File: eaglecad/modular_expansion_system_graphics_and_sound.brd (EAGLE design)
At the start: 90.2 x 100 mm, 44 parts, among them IC1 74LS244N, IC8 74LS244N, IC9-74HCU04 74LS04N, J1-WAIT-AND-INT WAIT-AND-INT, J1_ADDRESS_CON j1, J2_DATA_AND_POWER_CON j2, J3-VIDEO-OUT RCA, J4-AUDIO-LEFT RCA, J5-AUDIO-RIGHT RCA, Q2 2N2222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

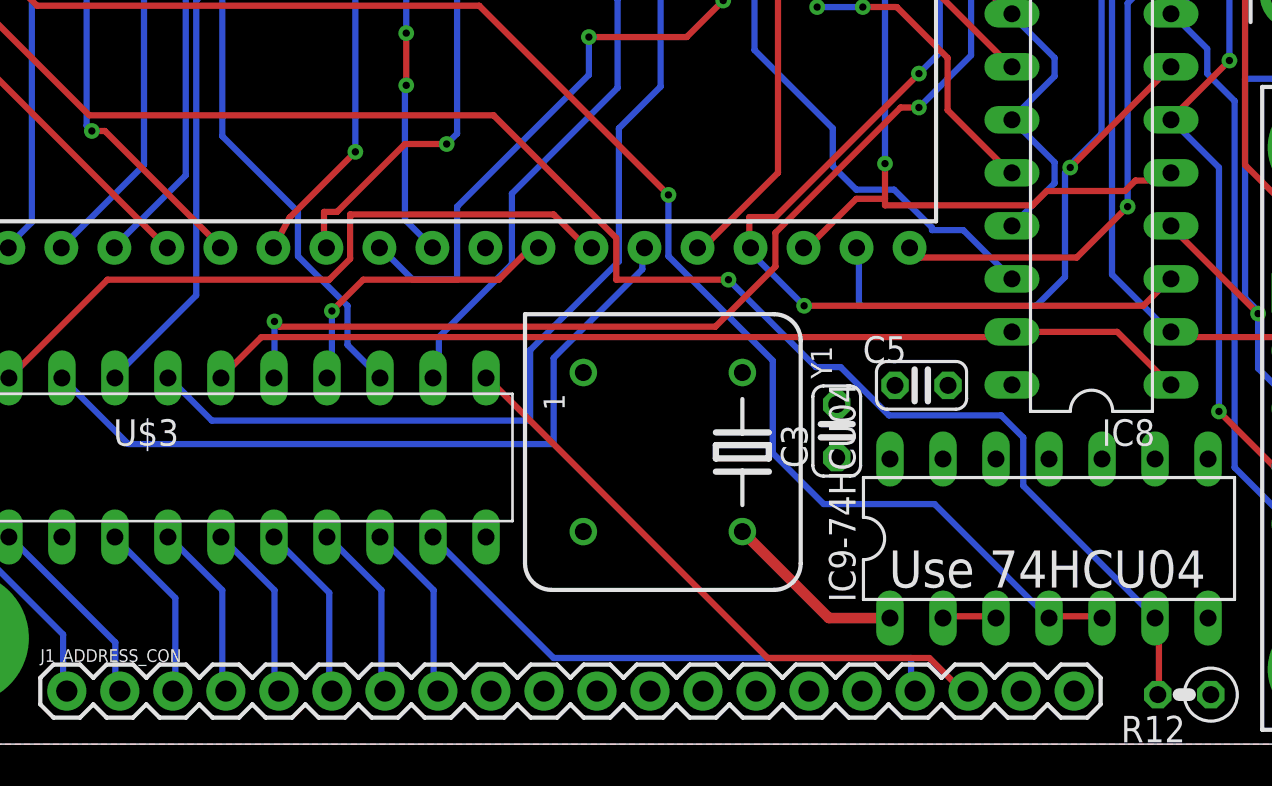
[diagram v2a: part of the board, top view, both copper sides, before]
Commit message: moved traces away from crystal module
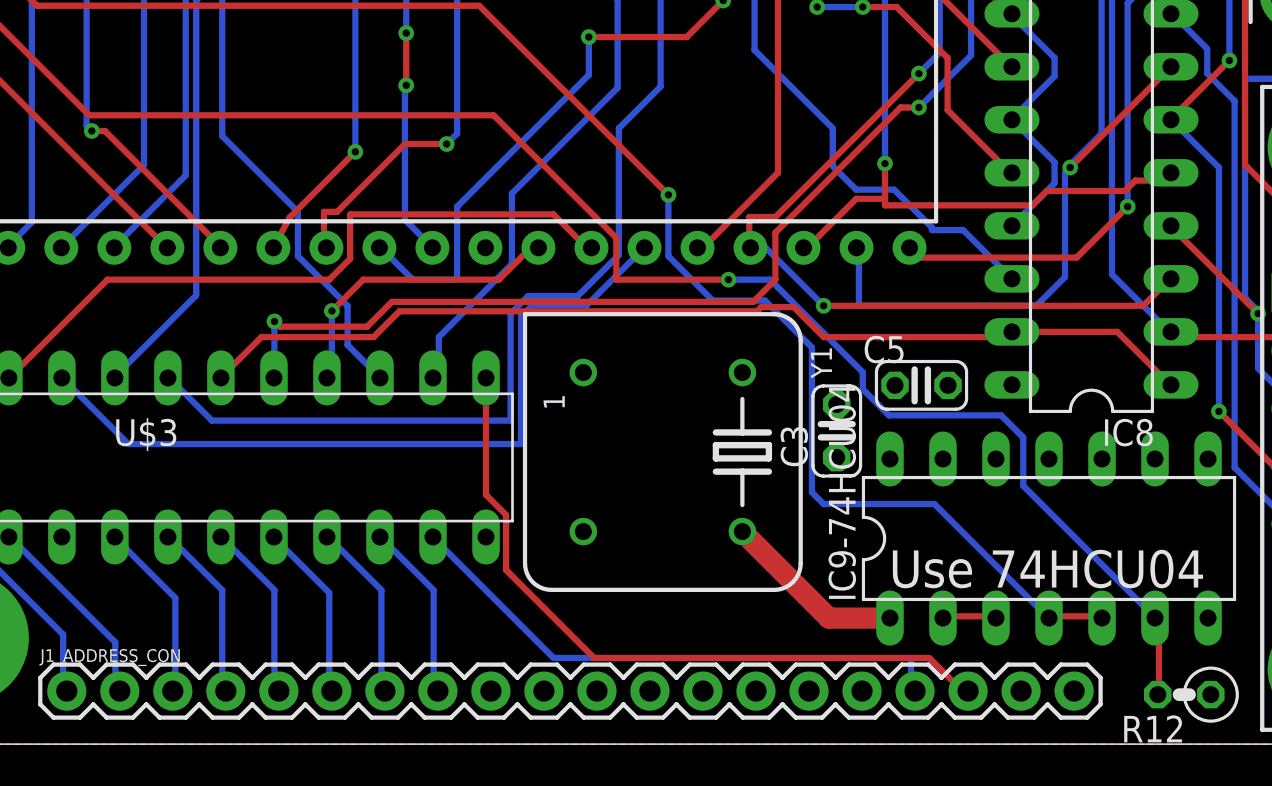
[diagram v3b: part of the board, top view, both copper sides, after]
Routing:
- net OUT*: track 29.3 -> 34.1 mm
- net CLK-IN-2: track 75.9 -> 77.3 mm
- net JOY1_IN_ENABLE_N: track 47.5 -> 48.7 mm
- net SND2_ENABLE_N: track 98.5 -> 99.3 mm
- net N$15: track 36.1 -> 36.7 mm
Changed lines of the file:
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@@
 <contactref element="J2_DATA_AND_POWER_CON" pad="20"/>
 <wire x1="70.625" y1="21" x2="71.875" y2="22.25" width="0.3" layer="1"/>
-<wire x1="54.375" y1="21" x2="70.625" y2="21" width="0.3" layer="1"/>
-<wire x1="51.875" y1="23.5" x2="54.375" y2="21" width="0.3" layer="16"/>
-<wire x1="51.875" y1="23.75" x2="51.875" y2="23.5" width="0.3" layer="16"/>
+<wire x1="55.3125" y1="21" x2="70.625" y2="21" width="0.3" layer="1"/>
+<wire x1="55.3125" y1="21" x2="52.535" y2="23.7775" width="0.3" layer="16"/>
+<wire x1="51.8075" y1="23.7775" x2="52.535" y2="23.7775" width="0.3" layer="16"/>
 <wire x1="71.875" y1="22.25" x2="71.9525" y2="22.29" width="0.3" layer="1"/>
-<wire x1="51.875" y1="23.75" x2="51.8075" y2="23.7775" width="0.3" layer="16"/>
 <wire x1="32.625" y1="68.625" x2="33.875" y2="67.375" width="0.3" layer="16"/>
 <wire x1="32.625" y1="78" x2="32.625" y2="68.625" width="0.3" layer="16"/>
@@
 <wire x1="51.75" y1="23.875" x2="51.8075" y2="23.7775" width="0.3" layer="1"/>
 <wire x1="64.125" y1="59.875" x2="64.14" y2="59.9175" width="0.3" layer="1"/>
-<via x="54.375" y="21" extent="1-16" drill="0.35"/>
+<via x="55.3125" y="21" extent="1-16" drill="0.35"/>
 <via x="65.75" y="85" extent="1-16" drill="0.35"/>
 <via x="59.875" y="32.125" extent="1-16" drill="0.35"/>
@@
 <contactref element="U$3" pad="18"/>
 <wire x1="28.375" y1="19.5" x2="26.5" y2="17.625" width="0.3" layer="1"/>
-<wire x1="64" y1="19.5" x2="28.375" y2="19.5" width="0.3" layer="1"/>
+<wire x1="64" y1="19.5" x2="56.25" y2="19.5" width="0.3" layer="1"/>
+<wire x1="56.25" y1="19.5" x2="55.3125" y2="19.5" width="0.3" layer="1"/>
+<wire x1="33.75" y1="19.5" x2="28.375" y2="19.5" width="0.3" layer="1"/>
 <wire x1="64.25" y1="19.75" x2="64" y2="19.5" width="0.3" layer="1"/>
 <wire x1="26.5" y1="17.625" x2="26.435" y2="17.5425" width="0.3" layer="1"/>
@@
 <wire x1="64.3325" y1="19.75" x2="69.375" y2="19.75" width="0.3" layer="1"/>
 <wire x1="71.875" y1="17.25" x2="71.9525" y2="17.21" width="0.3" layer="1"/>
+<wire x1="55.3125" y1="19.5" x2="53.875" y2="20.9375" width="0.3" layer="1"/>
+<wire x1="52.32729375" y1="20.9375" x2="52.12489375" y2="20.7351" width="0.3" layer="1"/>
+<wire x1="34.9851" y1="20.7351" x2="33.75" y2="19.5" width="0.3" layer="1"/>
+<wire x1="52.12489375" y1="20.7351" x2="34.9851" y2="20.7351" width="0.3" layer="1"/>
+<wire x1="53.875" y1="20.9375" x2="52.32729375" y2="20.9375" width="0.3" layer="1"/>
 </signal>
 <signal name="IN*">
@@
 <contactref element="J1_ADDRESS_CON" pad="18"/>
 <contactref element="U$3" pad="13"/>
-<wire x1="52.625" y1="4.125" x2="39.25" y2="17.5" width="0.3" layer="1"/>
-<wire x1="60.375" y1="4.125" x2="52.625" y2="4.125" width="0.3" layer="1"/>
+<wire x1="60.375" y1="4.125" x2="52.8125" y2="4.125" width="0.3" layer="1"/>
+<wire x1="52.8125" y1="4.125" x2="52.625" y2="4.125" width="0.3" layer="1"/>
 <wire x1="61.875" y1="2.625" x2="60.375" y2="4.125" width="0.3" layer="1"/>
 <wire x1="62.125" y1="2.625" x2="61.875" y2="2.625" width="0.3" layer="1"/>
-<wire x1="39.25" y1="17.5" x2="39.135" y2="17.5425" width="0.3" layer="1"/>
 <wire x1="62.125" y1="2.625" x2="62.23" y2="2.54" width="0.3" layer="1"/>
+<wire x1="52.625" y1="4.125" x2="44.3125" y2="4.125" width="0.3" layer="1"/>
+<wire x1="39.135" y1="11.94450625" x2="39.135" y2="17.5425" width="0.3" layer="1"/>
+<wire x1="40.0978" y1="8.3397" x2="40.0978" y2="10.98170625" width="0.3" layer="1"/>
+<wire x1="40.0978" y1="10.98170625" x2="39.135" y2="11.94450625" width="0.3" layer="1"/>
+<wire x1="44.3125" y1="4.125" x2="40.0978" y2="8.3397" width="0.3" layer="1"/>
 </signal>
 <signal name="VDP_MODE">
@@
 <contactref element="U$3" pad="21"/>
 <wire x1="22" y1="14.375" x2="18.875" y2="17.5" width="0.3" layer="16"/>
-<wire x1="42.375" y1="14.375" x2="22" y2="14.375" width="0.3" layer="16"/>
-<wire x1="42.375" y1="18.5" x2="42.375" y2="14.375" width="0.3" layer="16"/>
-<wire x1="46.625" y1="22.75" x2="42.375" y2="18.5" width="0.3" layer="16"/>
-<wire x1="46.625" y1="23.75" x2="46.625" y2="22.75" width="0.3" layer="16"/>
+<wire x1="22" y1="14.375" x2="40.8125" y2="14.375" width="0.3" layer="16"/>
+<wire x1="46.625" y1="23.6875" x2="46.625" y2="23.75" width="0.3" layer="16"/>
 <wire x1="18.875" y1="17.5" x2="18.815" y2="17.5425" width="0.3" layer="16"/>
 <wire x1="46.625" y1="23.75" x2="46.7275" y2="23.7775" width="0.3" layer="16"/>
+<wire x1="40.8125" y1="20.48520625" x2="41.34364375" y2="21.01635" width="0.3" layer="16"/>
+<wire x1="41.34364375" y1="21.01635" x2="43.95385" y2="21.01635" width="0.3" layer="16"/>
+<wire x1="40.8125" y1="14.375" x2="40.8125" y2="20.48520625" width="0.3" layer="16"/>
+<wire x1="43.95385" y1="21.01635" x2="46.625" y2="23.6875" width="0.3" layer="16"/>
 </signal>
 <signal name="UP1">
@@
 <wire x1="29" y1="20.25" x2="29" y2="17.625" width="0.3" layer="16"/>
 <wire x1="29.25" y1="20" x2="29" y2="20.25" width="0.3" layer="1"/>
-<wire x1="50.125" y1="20" x2="29.25" y2="20" width="0.3" layer="1"/>
-<wire x1="53" y1="22.875" x2="50.125" y2="20" width="0.3" layer="1"/>
-<wire x1="53" y1="24.5" x2="53" y2="22.875" width="0.3" layer="1"/>
+<wire x1="33.4375" y1="20" x2="29.25" y2="20" width="0.3" layer="1"/>
+<wire x1="53" y1="22.25" x2="51.9375" y2="21.1875" width="0.3" layer="1"/>
+<wire x1="53" y1="24.5" x2="53" y2="22.25" width="0.3" layer="1"/>
 <wire x1="59" y1="30.5" x2="53" y2="24.5" width="0.3" layer="1"/>
 <wire x1="59.875" y1="30.5" x2="59" y2="30.5" width="0.3" layer="1"/>
@@
 <via x="29" y="20.25" extent="1-16" drill="0.35"/>
 <via x="59.875" y="30.5" extent="1-16" drill="0.35"/>
+<wire x1="51.9375" y1="21.1875" x2="34.625" y2="21.1875" width="0.3" layer="1"/>
+<wire x1="34.625" y1="21.1875" x2="33.4375" y2="20" width="0.3" layer="1"/>
 </signal>
 <signal name="SND1_ENABLE_N">
@@
 <contactref element="U$3" pad="19"/>
 <wire x1="26" y1="15.5" x2="24" y2="17.5" width="0.3" layer="16"/>
-<wire x1="41.25" y1="15.5" x2="26" y2="15.5" width="0.3" layer="16"/>
-<wire x1="41.25" y1="18.875" x2="41.25" y2="15.5" width="0.3" layer="16"/>
-<wire x1="45.5" y1="23.125" x2="41.25" y2="18.875" width="0.3" layer="16"/>
-<wire x1="45.5" y1="29.5" x2="45.5" y2="23.125" width="0.3" layer="16"/>
+<wire x1="26" y1="15.5" x2="40.3125" y2="15.5" width="0.3" layer="16"/>
+<wire x1="43.53125" y1="21.46875" x2="45.5" y2="23.4375" width="0.3" layer="16"/>
+<wire x1="45.5" y1="23.4375" x2="45.5" y2="29.5" width="0.3" layer="16"/>
 <wire x1="47.5" y1="31.5" x2="45.5" y2="29.5" width="0.3" layer="16"/>
 <wire x1="47.5" y1="36.125" x2="47.5" y2="31.5" width="0.3" layer="16"/>
@@
 <wire x1="41.40625" y1="43.59375" x2="41.40625" y2="46.71875" width="0.3" layer="16"/>
 <wire x1="41.40625" y1="46.71875" x2="39.375" y2="48.75" width="0.3" layer="16"/>
+<wire x1="40.3125" y1="20.625" x2="41.15625" y2="21.46875" width="0.3" layer="16"/>
+<wire x1="41.15625" y1="21.46875" x2="43.53125" y2="21.46875" width="0.3" layer="16"/>
+<wire x1="40.3125" y1="15.5" x2="40.3125" y2="20.625" width="0.3" layer="16"/>
 </signal>
 <signal name="VID_RESET*">
@@
 <wire x1="60.625" y1="11.5" x2="66" y2="6.125" width="0.3" layer="16"/>
 <wire x1="60.625" y1="11.5" x2="55.3125" y2="11.5" width="0.3" layer="16"/>
-<wire x1="52.875" y1="18.375" x2="47.875" y2="23.375" width="0.3" layer="16"/>
+<wire x1="50" y1="21.25" x2="47.875" y2="23.375" width="0.3" layer="16"/>
 <wire x1="47.875" y1="26.3125" x2="47.875" y2="23.375" width="0.3" layer="16"/>
 <wire x1="38.8125" y1="35.375" x2="47.875" y2="26.3125" width="0.3" layer="1"/>
@@
 <wire x1="13.875" y1="39" x2="13.7075" y2="39.0175" width="0.3" layer="1"/>
 <via x="47.875" y="26.3125" extent="1-16" drill="0.35"/>
-<wire x1="55.3125" y1="11.5" x2="52.875" y2="13.9375" width="0.3" layer="16"/>
-<wire x1="52.875" y1="13.9375" x2="52.875" y2="18.375" width="0.3" layer="16"/>
+<wire x1="55.3125" y1="11.5" x2="54.75" y2="12.0625" width="0.3" layer="16"/>
+<wire x1="54.75" y1="19" x2="52.5" y2="21.25" width="0.3" layer="16"/>
+<wire x1="52.5" y1="21.25" x2="50" y2="21.25" width="0.3" layer="16"/>
+<wire x1="54.75" y1="12.0625" x2="54.75" y2="19" width="0.3" layer="16"/>
 </signal>
 <signal name="CLK-IN-1">
@@
 <wire x1="45.375" y1="22.25" x2="45.375" y2="24.25" width="0.3" layer="1"/>
 <wire x1="50.75" y1="22.25" x2="45.375" y2="22.25" width="0.3" layer="1"/>
-<wire x1="54.9375" y1="18.0625" x2="50.75" y2="22.25" width="0.3" layer="16"/>
 <wire x1="64.875" y1="12.375" x2="64.875" y2="14.6875" width="0.3" layer="16"/>
 <wire x1="71.125" y1="6.125" x2="64.875" y2="12.375" width="0.3" layer="16"/>
@@
 <wire x1="64.875" y1="14.6875" x2="63.8125" y2="15.75" width="0.3" layer="16"/>
 <wire x1="63.8125" y1="15.75" x2="58.4375" y2="15.75" width="0.3" layer="16"/>
-<wire x1="58.4375" y1="15.75" x2="56.125" y2="18.0625" width="0.3" layer="16"/>
-<wire x1="56.125" y1="18.0625" x2="54.9375" y2="18.0625" width="0.3" layer="16"/>
+<wire x1="52.75" y1="22.25" x2="50.75" y2="22.25" width="0.3" layer="16"/>
+<wire x1="58.4375" y1="15.75" x2="57.1875" y2="17" width="0.3" layer="16"/>
+<wire x1="57.1875" y1="17" x2="57.1875" y2="17.8125" width="0.3" layer="16"/>
+<wire x1="57.1875" y1="17.8125" x2="52.75" y2="22.25" width="0.3" layer="16"/>
 </signal>
 <signal name="N$12">
@@
 <contactref element="Y1" pad="5"/>
 <contactref element="IC9-74HCU04" pad="1"/>
-<wire x1="58.4875" y1="6.04" x2="55.56" y2="6.04" width="0.508" layer="1"/>
-<wire x1="55.56" y1="6.04" x2="51.4175" y2="10.1825" width="0.508" layer="1"/>
+<wire x1="58.4875" y1="6.04" x2="55.56" y2="6.04" width="1.016" layer="1"/>
+<wire x1="55.56" y1="6.04" x2="51.4175" y2="10.1825" width="1.016" layer="1"/>
 </signal>
 <signal name="N$5">
